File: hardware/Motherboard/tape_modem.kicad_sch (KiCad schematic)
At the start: 1 part, among them U66 74LS273

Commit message: wip
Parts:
- removed U66: 74LS273, symbol 74xx:74LS273
- added U69: MC6850, Package_DIP:DIP-24_W15.24mm, symbol Interface_UART:MC6850
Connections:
- net PD0: now also U69.22 (D0)
- net PD1: now also U69.21 (D1)
- net PD2: now also U69.20 (D2)
- net PD3: now also U69.19 (D3)
- net PD4: now also U69.18 (D4)
- net PD5: now also U69.17 (D5)
- net PD6: now also U69.16 (D6)
- net PD7: now also U69.15 (D7)
- net VCC5V: now also U69.10 (CS1), U69.12 (VCC), U69.8 (CS0)
- net VSS: now also U69.1 (VSS)
- new net EB: U69.14 (E)
- new net PA0: U69.11 (RS)
- new net R~{W}B: U69.13 (R/~{W})
- new net ~{CS_ACIA}: U69.9 (CS2)
- no-connect marks 0 -> 1

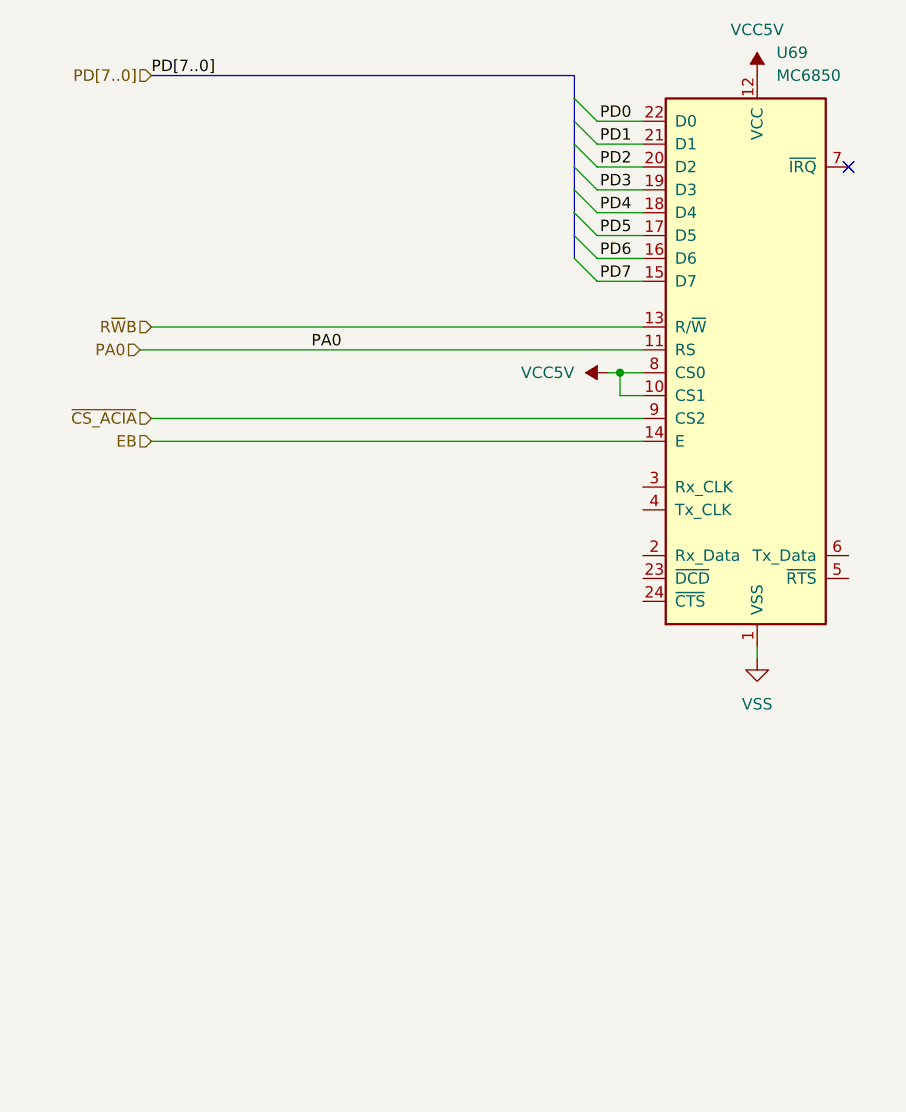
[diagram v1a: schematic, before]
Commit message: S30 bus + annotations fixes.
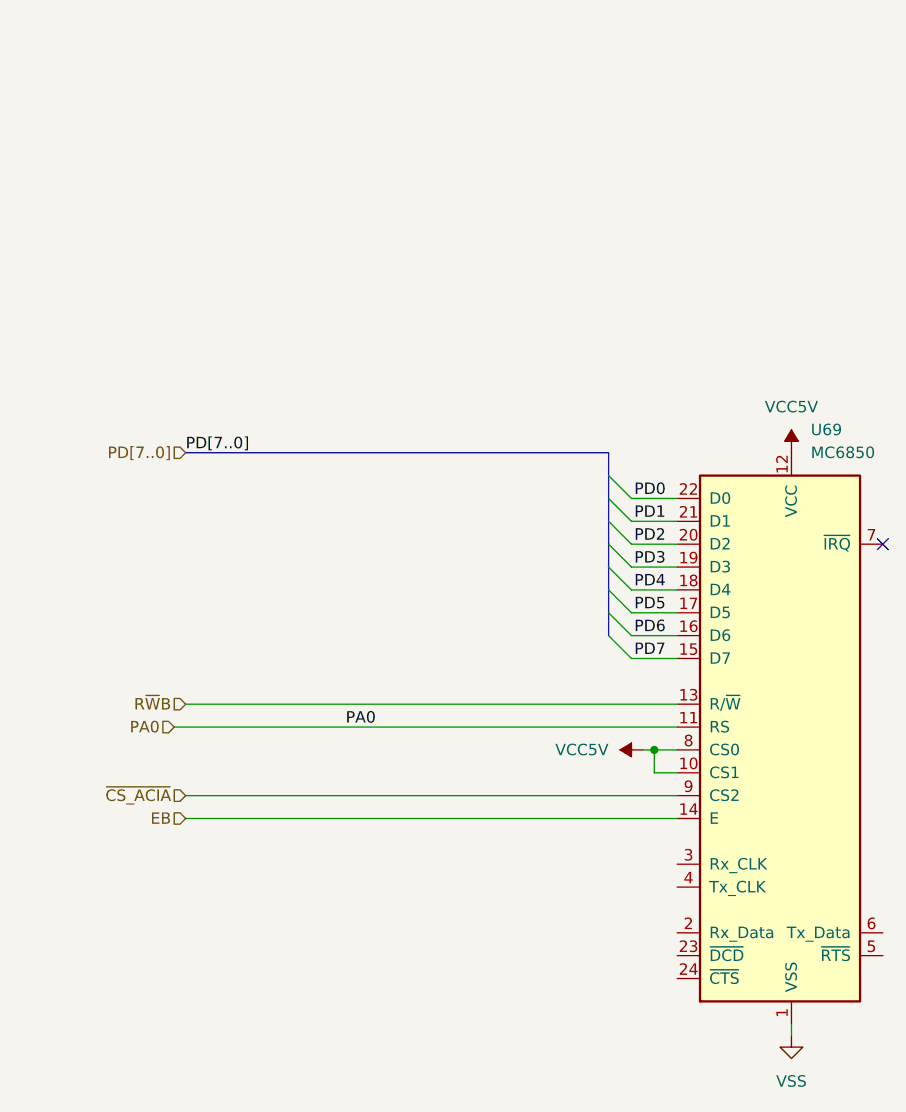
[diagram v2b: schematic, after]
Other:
- title: (none) -> Apollo 7 Squale - Tape & modem interfaces
- moved on the sheet: U69

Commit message: wip : modem
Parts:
- added C5: 22pF, symbol Device:C
- added C6: 10pF, symbol Device:C
- added U67: TL084, symbol Amplifier_Operational:TL084
- added U68: EFB7510, symbol Interface_Telecom:FX614
- added U70: 74LS02, symbol 74xx:74LS02
- added U71: 74LS393, symbol 74xx:74LS393
- added Y2: 3.579MHz, symbol Device:Crystal
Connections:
- net VCC5V: now also U68.1 (V+), U70.14 (VCC), U71.14 (VCC)
- net VSS: now also C5.2, C6.1, U68.3 (GNDD), U68.8 (GNDA), U70.7 (GND), U71.2 (MR), U71.7 (GND)
- net at U69.2 (Rx_Data): now also U68.11 (RXD)
- net at U69.23 (~{DCD}): now also U68.12 (~{DCD})
- net at U69.3 (Rx_CLK): now also U68.16 (RxCLK), U70.3, U71.1 (CP)
- net at U69.4 (Tx_CLK): now also U70.4
- net at U69.5 (~{RTS}): now also U68.2 (~{RTS})
- net at U69.6 (Tx_Data): now also U68.17 (TXD)
- new net: C5.1, U68.15 (XTAL_IN), Y2.1
- new net: C6.2, U68.14 (XTAL_OUT), Y2.2
- new net: U70.10, U70.5
- new net: U70.1, U70.6
- new net: U70.9, U71.6 (Q3)
- new net: U70.13, U70.2
- new net SYS_MDM_MC_~{BC}: U68.18 (MC/~{BC}), U70.11, U70.12, U70.8
- new net VEE5V: U68.6 (V-)
- no-connect marks 1 -> 4
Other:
- moved on the sheet: U69

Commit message: wip
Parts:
- added C10: 68pF, symbol Device:C
- added C11, C12, C9: 100nF, symbol Device:C
- added D1, D2: 1N4148, Diode_THT:D_DO-35_SOD27_P7.62mm_Horizontal, symbol Diode:1N4148
- added R23, R26, R29, R30, R33, R34: 10K, symbol Device:R
- added R24: 330K, symbol Device:R
- added R25, R27: 47K, symbol Device:R
- added R28: 33K3, symbol Device:R
- added R31, R47: 470R, symbol Device:R
- added R32: 2K2, symbol Device:R
- added R36: 4K7, symbol Device:R
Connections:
- net VSS: now also U67.10 (+), U67.12 (+), U67.3 (+), R25.2, R47.1
- net at U67.1: now also R28.1, R29.2, R31.2, R33.1
- net at U67.2 (-): now also R28.2, R32.1
- net at U68.13 (RDI): now also U67.14, R27.1
- net at U68.5 (RFO): now also R23.1
- net at U68.7 (RAI): now also U67.7, R30.1
- net at U67.5 (+): now also R31.1
- net at U67.6 (-): now also R29.1, R30.2, R36.1
- net at U67.13 (-): now also R26.1, R27.2
- net at U67.8: now also C10.1, C11.2, R24.1
- net at U67.9 (-): now also C10.2, C9.2, D1.1 (K), D2.2 (A), R24.2
- new net: C11.1, C12.2, D1.2 (A), D2.1 (K), R25.1
- new net: R33.2, R34.1
- new net: C12.1, R26.2
- new net: C9.1, R23.2
- new net: R34.2, R47.2
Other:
- moved on the sheet: U67A, U67B, U67E

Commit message: wip: tape / modem interface.
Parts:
- added C13: 100nF, symbol Device:C
- added J5: DIN-5_180degree, symbol Connector:DIN-5_180degree
- added J6: DE9_Socket, symbol Connector:DE9_Socket
- added P1: VR10K, symbol Device:R_Potentiometer
- added R35, R37: 10K, symbol Device:R
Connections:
- net SYS_MDM_LINE: now also J6.1
- net VCC5V: now also U67.4 (V+), J6.3
- net VEE5V: now also U67.11 (V-)
- net VSS: now also U69.24 (~{CTS}), J5.2, J6.5, J6.8, P1.3, R37.1
- net IN_1: now reaches R36.2
- net IN_1: now also J5.3, R35.1, R37.2
- net OUT_1V_LEVEL: now reaches R33.2, R34.1
- net OUT_1V_LEVEL: now also J5.4
- net MDM_CLK_19K2: now reaches U68.16 (RxCLK), U69.3 (Rx_CLK), U70.3, U71.1 (CP)
- net MDM_CLK_TX: now reaches U69.4 (Tx_CLK), U70.4
- net at R28.2, U67.2 (-): now also R32.2; no longer R32.1
- net at R31.1, U67.5 (+): now also J6.4
- net at U68.10 (VREF): now also P1.1
- net at U68.4 (ATO): now also C13.2
- net at U68.9 (RSA): now also P1.2
- net OUT_50mV_LEVEL: now reaches R34.2, R47.2
- net OUT_50mV_LEVEL: now also J5.1
- new net: C13.1, R32.1
- new net IN_2: J5.5, R35.2
- new net MODEM_RING: J6.2
- no-connect marks 4 -> 7
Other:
- note added: "(1200 Hz -> 75 Baud) (19200 Hz -> 1200 Baud)"
- note added: "/ 22.28 -26.95 dB"
- note added: "Duplexer"
- note added: "G = 33K3/2K2 = * 15,14 20 * log 15,14 = +23,6 dB"
- note added: "G = 47K/10K = 4,7 20 * log 4,7 = 13,44 dB"
- note added: "High pass filter Cutoff frequency (-3 dB) : fc = 1 / ( 2 * PI * 10K * 100nF ) = 159.15 Hz"
- note added: "Low pass filter G = 330K/10K = 33 20 * log 33 = 30,37 dB Cutoff frequency (-3 dB) : fc = 1 / ( 2 * PI * 330K * 68pF ) = 7092.47 Hz"
- note added: "Peak limiter band pass filter"
- note added: "Peak limiter band pass filter curve"
- note added: "RxCLK divisor 19200Hz / 16 = 1200 Hz (1200 Hz -> 75 Baud)"
- note added: "TX Clock source selector. SYS_MDM_MC_~{BC} Low : 1200 Hz (75 Baud) SYS_MDM_MC_~{BC} High : 19200 Hz (1200 Baud)"
- note added: "TX baudrate selection Low = 75 baud High = 1200 baud."
- note added: "max level : +8 dBm (< 6 VPP)"
- note added: "peak limiter (1V)"
- moved on the sheet: C10, C11, C12, C5, C6, C9, D1, D2, R23, R24, R26, R27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

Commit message: R32 and R36 values fixed. Gain fixed.
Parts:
- R32: value 2K2 -> 22K
- R36: value 4K7 -> 47K
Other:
- note added: "G = 33K3/22K = * 1.514 20 * log 1.514 = +3,6 dB"
- note removed: "G = 33K3/2K2 = * 15,14 20 * log 15,14 = +23,6 dB"
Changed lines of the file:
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@@
 		)
 	)
-	(text "G = 33K3/2K2 = * 15,14\n20 * log 15,14 = +23,6 dB"
+	(text "G = 33K3/22K = * 1.514\n20 * log 1.514 = +3,6 dB"
 		(exclude_from_sim no)
 		(at 301.752 22.606 0)
@@
 			)
 		)
-		(property "Value" "4K7"
+		(property "Value" "47K"
 			(at 326.136 70.612 90)
 			(effects
@@
 			)
 		)
-		(property "Value" "2K2"
+		(property "Value" "22K"
 			(at 285.75 33.02 90)
 			(effects

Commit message: signals levels.
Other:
- note added: "+/- 1.20V"
- note added: "+/- 2.36V"
- note added: "+/- 54mV"
- note added: "Typical output level : +/- 1.56V"
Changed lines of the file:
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@@
 		(comment 3 "Drawn by Jean-François DEL NERO")
+	)
+	(text "+/- 1.20V"
+		(exclude_from_sim no)
+		(at 357.632 28.194 0)
+		(effects
+			(font
+				(size 1.27 1.27)
+			)
+		)
+	)
+	(text "Typical output level : +/- 1.56V"
+		(exclude_from_sim no)
+		(at 264.922 65.024 90)
+		(effects
+			(font
+				(size 1.27 1.27)
+			)
+		)
 	)
 	(text "Peak limiter band pass filter"
@@
 	(text "Duplexer"
 		(exclude_from_sim no)
-		(at 322.326 50.292 0)
+		(at 308.356 63.5 0)
 		(effects
 			(font
@@
 			)
 			(justify left)
+		)
+	)
+	(text "+/- 54mV"
+		(exclude_from_sim no)
+		(at 357.632 37.338 0)
+		(effects
+			(font
+				(size 1.27 1.27)
+			)
 		)
 	)
@@
 		)
 	)
+	(text "+/- 2.36V"
+		(exclude_from_sim no)
+		(at 314.96 51.816 90)
+		(effects
+			(font
+				(size 1.27 1.27)
+			)
+		)
+	)
